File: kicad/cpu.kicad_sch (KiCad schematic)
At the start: 20 parts, among them IC1 Z8-L180-S180-180-PLCC-68, U16 74HC00, U20 74HC688, U21 74HC688, U23 74HC74, U27 74HC32, U8 74HC138, Y2 16 MHz

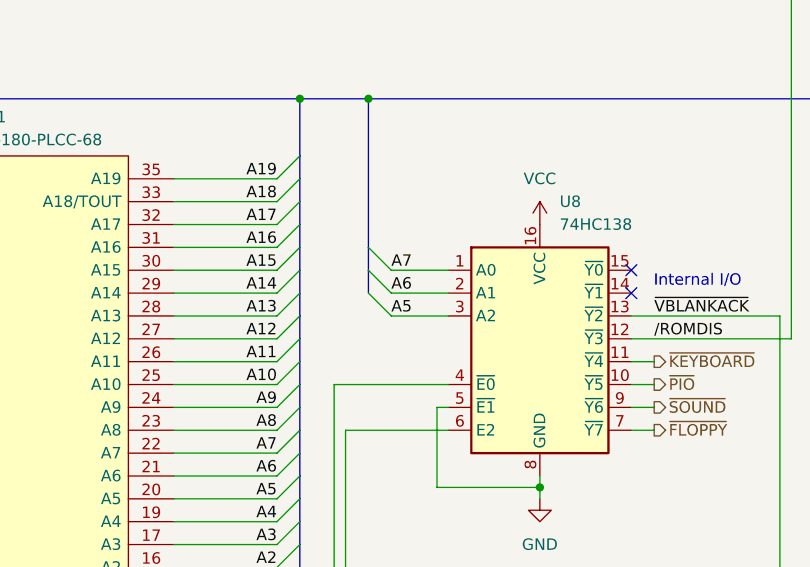
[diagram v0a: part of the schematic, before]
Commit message: HW: Fix bug in I/O decoder
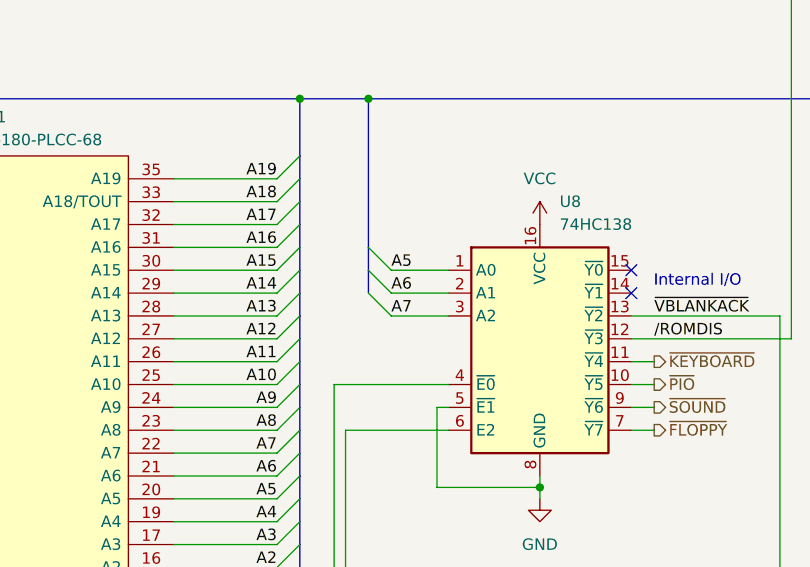
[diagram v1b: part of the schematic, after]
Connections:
- net A5: now also U8.1 (A0); no longer U8.3 (A2)
- net A7: now also U8.3 (A2); no longer U8.1 (A0)
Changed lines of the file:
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@@
 		)
 	)
-	(label "A5"
+	(label "A7"
 		(at 146.05 58.42 0)
 		(fields_autoplaced yes)
@@
 		)
 	)
-	(label "A7"
+	(label "A5"
 		(at 146.05 53.34 0)
 		(fields_autoplaced yes)

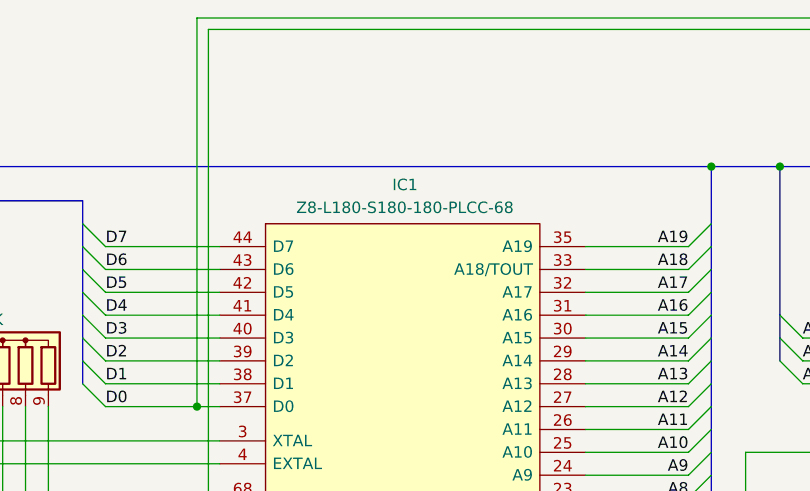
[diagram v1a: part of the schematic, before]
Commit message: HW: Fix A0 of AY-3-8912 being connected to D0 instead of A0
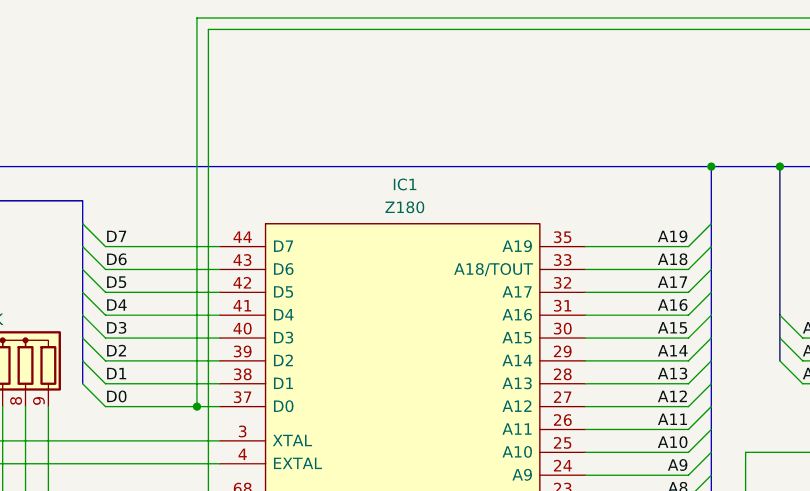
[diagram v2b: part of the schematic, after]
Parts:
- IC1: value Z8-L180-S180-180-PLCC-68 -> Z180
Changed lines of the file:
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@@
 			)
 		)
-		(property "Value" "Z8-L180-S180-180-PLCC-68"
+		(property "Value" "Z180"
 			(at 101.854 38.862 0)
 			(effects

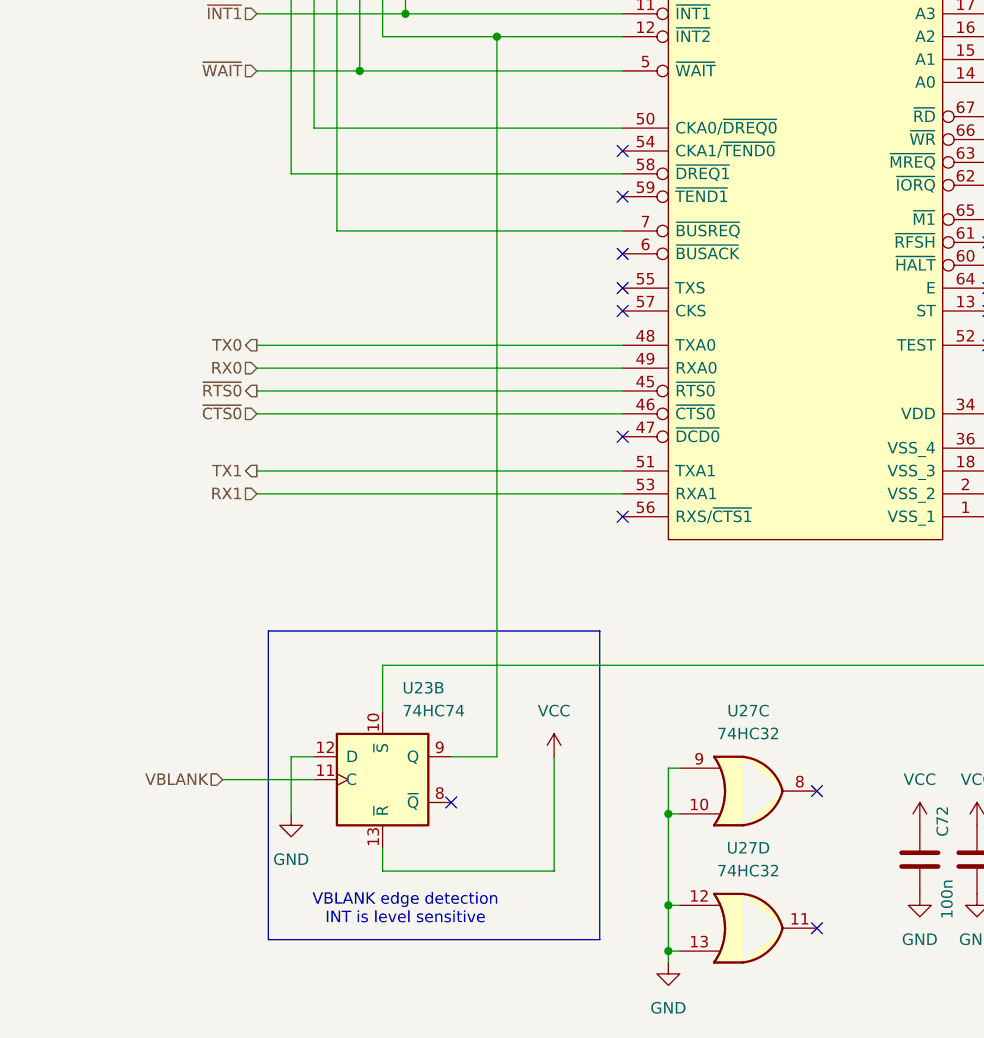
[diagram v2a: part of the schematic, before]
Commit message: HW: Connect 82077 /DREQ to the Z180 DMA ch 1, PCB decorations
Rev B done
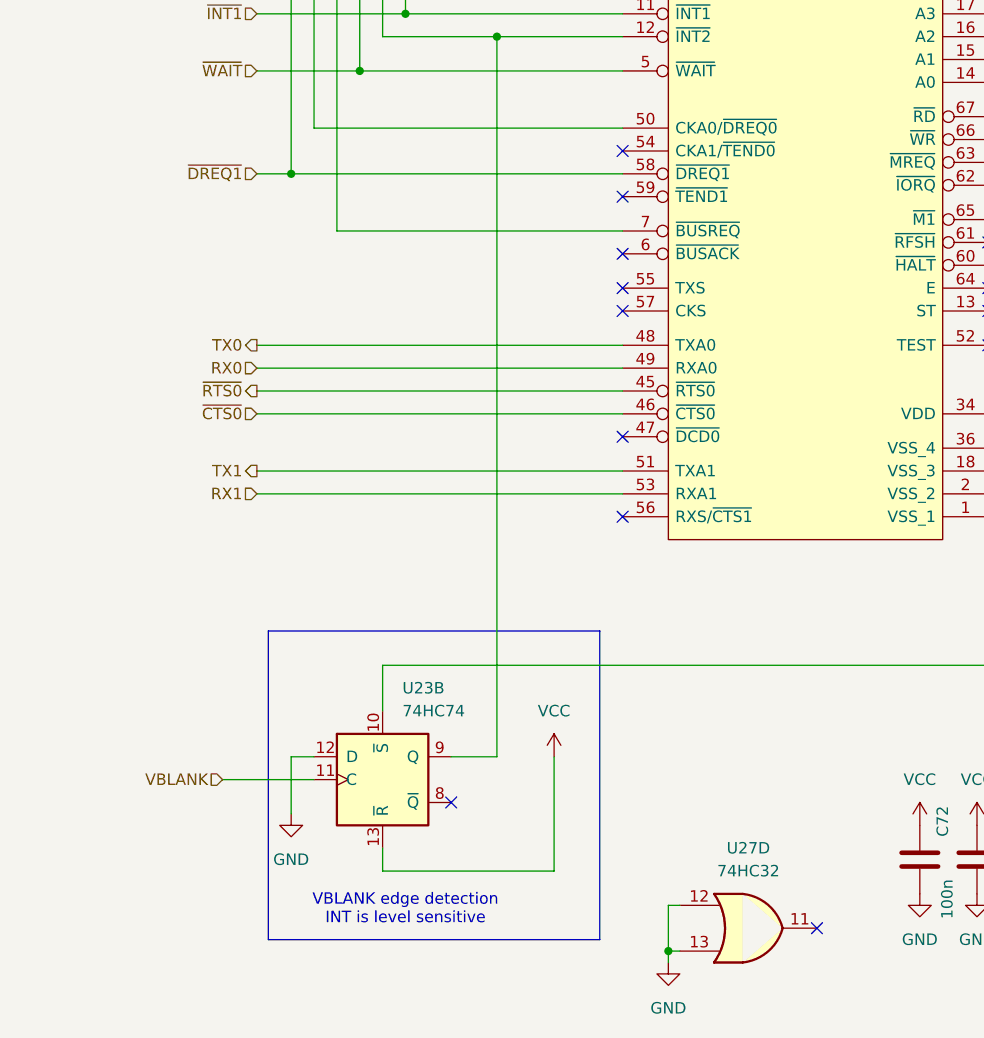
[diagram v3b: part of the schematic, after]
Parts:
- removed unit 3 of U27
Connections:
- net ~{DREQ1}: now reaches IC1.58 (~{DREQ1}), RN2.2 (R1)
- no-connect marks 17 -> 16
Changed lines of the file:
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@@
 	)
 	(junction
-		(at 86.36 172.72)
-		(diameter 0)
-		(color 0 0 0 0)
-	)
-	(junction
-		(at 86.36 182.88)
-		(diameter 0)
-		(color 0 0 0 0)
-	)
-	(junction
 		(at 62.23 78.74)
 		(diameter 0)
@@
 	)
 	(junction
+		(at 44.45 101.6)
+		(diameter 0)
+		(color 0 0 0 0)
+	)
+	(junction
 		(at 207.01 90.17)
 		(diameter 0)
@@
 		(at 121.92 116.84)
 	)
-	(no_connect
-		(at 102.87 170.18)
-	)
 	(bus_entry
 		(at 66.04 55.88)
@@
 	(wire
 		(pts
-			(xy 86.36 182.88) (xy 86.36 172.72)
-		)
-		(stroke
-			(width 0)
-			(type default)
-		)
-	)
-	(wire
-		(pts
 			(xy 200.66 130.81) (xy 203.2 130.81)
 		)
@@
 	(wire
 		(pts
-			(xy 86.36 172.72) (xy 86.36 167.64)
-		)
-		(stroke
-			(width 0)
-			(type default)
-		)
-	)
-	(wire
-		(pts
 			(xy 162.56 77.47) (xy 162.56 76.2)
 		)
@@
 	(wire
 		(pts
-			(xy 86.36 167.64) (xy 87.63 167.64)
-		)
-		(stroke
-			(width 0)
-			(type default)
-		)
-	)
-	(wire
-		(pts
 			(xy 200.66 74.93) (xy 203.2 74.93)
 		)
@@
 	(wire
 		(pts
-			(xy 86.36 172.72) (xy 87.63 172.72)
-		)
-		(stroke
-			(width 0)
-			(type default)
-		)
-	)
-	(wire
-		(pts
 			(xy 121.92 100.33) (xy 201.93 100.33)
 		)
@@
 	(wire
 		(pts
+			(xy 40.64 101.6) (xy 44.45 101.6)
+		)
+		(stroke
+			(width 0)
+			(type default)
+		)
+	)
+	(wire
+		(pts
 			(xy 255.27 46.99) (xy 241.3 46.99)
 		)
@@
 		)
 	)
+	(hierarchical_label "~{DREQ1}"
+		(shape input)
+		(at 40.64 101.6 180)
+		(fields_autoplaced yes)
+		(effects
+			(font
+				(size 1.27 1.27)
+			)
+			(justify right)
+		)
+	)
 	(hierarchical_label "~{WR}"
 		(shape output)
@@
 				)
 			)
-		)
-	)
-	(symbol
-		(lib_id "74xx:74LS32")
-		(at 95.25 170.18 0)
-		(unit 3)
-		(exclude_from_sim no)
-		(in_bom yes)
-		(on_board yes)
-		(dnp no)
-		(fields_autoplaced yes)
-		(property "Reference" "U27"
-			(at 95.25 161.29 0)
-			(effects
-				(font
-					(size 1.27 1.27)
-				)
-			)
-		)
-		(property "Value" "74HC32"
-			(at 95.25 163.83 0)
-			(effects
-				(font
-					(size 1.27 1.27)
-				)
-			)
-		)
-		(property "Footprint" "Package_DIP:DIP-14_W7.62mm"
-			(at 95.25 170.18 0)
-			(effects
-				(font
-					(size 1.27 1.27)
-				)
-				(hide yes)
-			)
-		)
-		(property "Datasheet" "http://www.ti.com/lit/gpn/sn74LS32"
-			(at 95.25 170.18 0)
-			(effects
-				(font
-					(size 1.27 1.27)
-				)
-				(hide yes)
-			)
-		)
-		(property "Description" "Quad 2-input OR"
-			(at 95.25 170.18 0)
-			(effects
-				(font
-					(size 1.27 1.27)
-				)
-				(hide yes)
-			)
-		)
-		(pin "12"
-		)
-		(pin "9"
-		)
-		(pin "3"
-		)
-		(pin "4"
-		)
-		(pin "10"
-		)
-		(pin "1"
-		)
-		(pin "13"
-		)
-		(pin "5"
-		)
-		(pin "14"
-		)
-		(pin "7"
-		)
-		(pin "2"
-		)
-		(pin "8"
-		)
-		(pin "11"
-		)
-		(pin "6"
-		)
-		(instances
-			(project ""
-				(path "/ca48b56d-33a4-442b-b1b9-aaf2c2c8d68d/f772451e-6b0a-44d2-8d0b-110d70bebcb8"
-					(reference "U27")
-					(unit 3)
-				)
-			)

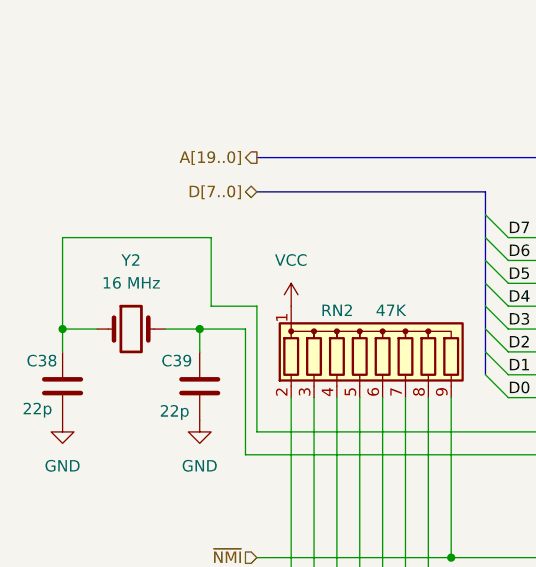
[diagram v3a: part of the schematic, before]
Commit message: HW: Fix unconnected /SOUND net, add /RST header and /DTR power supply
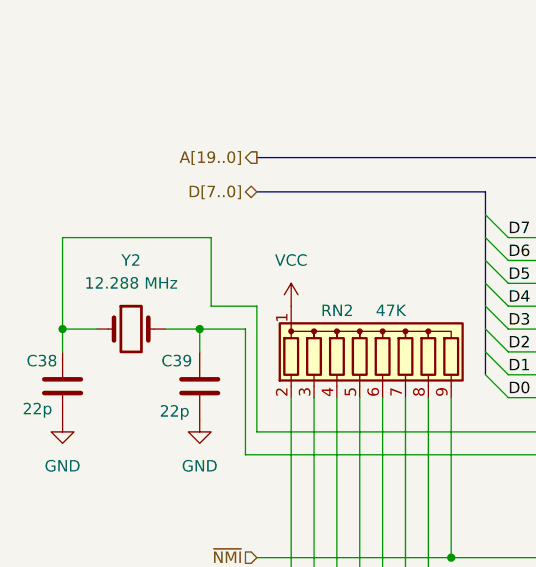
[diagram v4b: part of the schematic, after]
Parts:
- C38, C39: footprint Capacitor_THT:C_Disc_D4.3mm_W1.9mm_P5.00mm -> Capacitor_THT:C_Disc_D5.0mm_W2.5mm_P2.50mm
- Y2: value 16 MHz -> 12.288 MHz
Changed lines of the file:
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@@
 			)
 		)
-		(property "Value" "16 MHz"
+		(property "Value" "12.288 MHz"
 			(at 26.67 48.26 0)
 			(effects
@@
 			)
 		)
-		(property "Footprint" "Capacitor_THT:C_Disc_D4.3mm_W1.9mm_P5.00mm"
+		(property "Footprint" "Capacitor_THT:C_Disc_D5.0mm_W2.5mm_P2.50mm"
 			(at 33.3248 55.88 0)
 			(effects
@@
 			)
 		)
-		(property "Footprint" "Capacitor_THT:C_Disc_D4.3mm_W1.9mm_P5.00mm"
+		(property "Footprint" "Capacitor_THT:C_Disc_D5.0mm_W2.5mm_P2.50mm"
 			(at 18.0848 55.88 0)
 			(effects
